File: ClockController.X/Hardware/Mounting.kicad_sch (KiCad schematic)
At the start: 3 parts

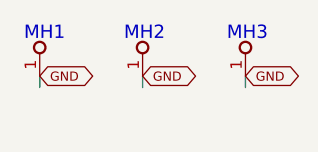
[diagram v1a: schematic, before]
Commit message: Replace the imported objects with native kicad equivalents
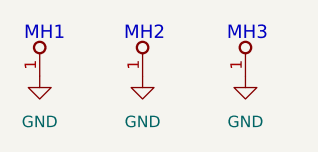
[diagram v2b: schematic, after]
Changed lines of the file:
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@@
-		)
-	)
-	(wire
-		(pts
-			(xy 157.48 105.41) (xy 157.48 106.68)
-		)
-		(stroke
-			(width 0.25)
-			(type solid)
-		)
-	)
-	(wire
-		(pts
-			(xy 146.05 105.41) (xy 146.05 106.68)
-		)
-		(stroke
-			(width 0.25)
-			(type solid)
-		)
-	)
-	(wire
-		(pts
-			(xy 134.62 105.41) (xy 134.62 106.68)
-		)
-		(stroke
-			(width 0.25)
-			(type solid)
-		)
-	)
-	(global_label "GND"
-		(shape bidirectional)
-		(at 134.62 105.41 0)
-		(fields_autoplaced yes)
-		(effects
-			(font
-				(size 1.016 1.016)
-			)
-			(justify left)
-		)
-		(property "Intersheetrefs" "${INTERSHEET_REFS}"
-			(at 140.9933 105.41 0)
-			(effects
-				(font
-					(size 1.27 1.27)
-				)
-				(justify left)
-				(hide yes)
-			)
-		)
-	)
-	(global_label "GND"
-		(shape bidirectional)
-		(at 157.48 105.41 0)
-		(fields_autoplaced yes)
-		(effects
-			(font
-				(size 1.016 1.016)
-			)
-			(justify left)
-		)
-		(property "Intersheetrefs" "${INTERSHEET_REFS}"
-			(at 163.8533 105.41 0)
-			(effects
-				(font
-					(size 1.27 1.27)
-				)
-				(justify left)
-				(hide yes)
-			)
-		)
-	)
-	(global_label "GND"
-		(shape bidirectional)
-		(at 146.05 105.41 0)
-		(fields_autoplaced yes)
-		(effects
-			(font
-				(size 1.016 1.016)
-			)
-			(justify left)
-		)
-		(property "Intersheetrefs" "${INTERSHEET_REFS}"
-			(at 152.4233 105.41 0)
-			(effects
-				(font
-					(size 1.27 1.27)
-				)
-				(justify left)
-				(hide yes)
-			)
 		)
 	)
@@
 					(unit 1)
 				)
+			)
+		)
+	)
+	(symbol
+		(lib_id "power:GND")
+		(at 157.48 105.41 0)
+		(unit 1)
+		(exclude_from_sim no)
+		(in_bom yes)
+		(on_board yes)
+		(dnp no)
+		(fields_autoplaced yes)
+		(property "Reference" "#PWR022"
+			(at 157.48 111.76 0)
+			(effects
+				(font
+					(size 1.27 1.27)
+				)
+				(hide yes)
+			)
+		)
+		(property "Value" "GND"
+			(at 157.48 110.49 0)
+			(effects
+				(font
+					(size 1.27 1.27)
+				)
+			)
+		)
+		(property "Footprint" ""
+			(at 157.48 105.41 0)
+			(effects
+				(font
+					(size 1.27 1.27)
+				)
+				(hide yes)
+			)
+		)
+		(property "Datasheet" ""
+			(at 157.48 105.41 0)
+			(effects
+				(font
+					(size 1.27 1.27)
+				)
+				(hide yes)
+			)
+		)
+		(property "Description" "Power symbol creates a global label with name \"GND\" , ground"
+			(at 157.48 105.41 0)
+			(effects
+				(font
+					(size 1.27 1.27)
+				)
+				(hide yes)
+			)
+		)
+		(pin "1"
+		)
+		(instances
+			(project ""
+				(path "/de4049ea-1674-4dcc-86d3-bb1be3dcf2e7/70fc2848-2605-4874-bf04-b4bbdf7c1213"
+					(reference "#PWR022")
+					(unit 1)
+				)
+			)
+		)
+	)
+	(symbol
+		(lib_id "power:GND")
+		(at 146.05 105.41 0)
+		(unit 1)
+		(exclude_from_sim no)
+		(in_bom yes)
+		(on_board yes)
+		(dnp no)
+		(fields_autoplaced yes)
+		(property "Reference" "#PWR021"
+			(at 146.05 111.76 0)
+			(effects
+				(font
+					(size 1.27 1.27)
+				)
+				(hide yes)
+			)
+		)
+		(property "Value" "GND"
+			(at 146.05 110.49 0)
+			(effects
+				(font
+					(size 1.27 1.27)
+				)
+			)
+		)
+		(property "Footprint" ""
+			(at 146.05 105.41 0)
+			(effects
+				(font
+					(size 1.27 1.27)
+				)
+				(hide yes)
+			)
+		)
+		(property "Datasheet" ""
+			(at 146.05 105.41 0)
+			(effects
+				(font
+					(size 1.27 1.27)
+				)
+				(hide yes)
+			)
+		)
+		(property "Description" "Power symbol creates a global label with name \"GND\" , ground"
+			(at 146.05 105.41 0)
+			(effects
+				(font
+					(size 1.27 1.27)
+				)
+				(hide yes)
+			)
+		)
+		(pin "1"
+		)
+		(instances
+			(project ""
+				(path "/de4049ea-1674-4dcc-86d3-bb1be3dcf2e7/70fc2848-2605-4874-bf04-b4bbdf7c1213"
+					(reference "#PWR021")
+					(unit 1)
+				)
+			)
+		)
+	)
+	(symbol
+		(lib_id "power:GND")
+		(at 134.62 105.41 0)
+		(unit 1)
+		(exclude_from_sim no)
+		(in_bom yes)
+		(on_board yes)
+		(dnp no)
+		(fields_autoplaced yes)
+		(property "Reference" "#PWR020"
+			(at 134.62 111.76 0)
+			(effects
+				(font
+					(size 1.27 1.27)
+				)
+				(hide yes)
+			)
+		)
+		(property "Value" "GND"
+			(at 134.62 110.49 0)
+			(effects
+				(font
+					(size 1.27 1.27)
+				)
+			)
+		)
+		(property "Footprint" ""
+			(at 134.62 105.41 0)
+			(effects
+				(font
+					(size 1.27 1.27)
+				)
+				(hide yes)
+			)
+		)
+		(property "Datasheet" ""
+			(at 134.62 105.41 0)
+			(effects
+				(font
+					(size 1.27 1.27)
+				)
+				(hide yes)
+			)
+		)
+		(property "Description" "Power symbol creates a global label with name \"GND\" , ground"
+			(at 134.62 105.41 0)
+			(effects
+				(font
+					(size 1.27 1.27)
+				)
+				(hide yes)
+			)
+		)
+		(pin "1"
+		)
+		(instances
+			(project ""
+				(path "/de4049ea-1674-4dcc-86d3-bb1be3dcf2e7/70fc2848-2605-4874-bf04-b4bbdf7c1213"
+					(reference "#PWR020")
+					(unit 1)
+				)
